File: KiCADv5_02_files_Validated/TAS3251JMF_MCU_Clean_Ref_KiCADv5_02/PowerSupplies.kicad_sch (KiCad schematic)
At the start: 47 parts, among them IC1 LM5010MHX, J18 Conn_01x04, J5 PVDD, J6 Conn_01x01_Male, J7 Conn_01x01_Male, J8 Conn_01x01_Male, J9 Conn_01x01_Male, U2 AMS1117-3.3, U3 LM2940-12

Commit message: adding components
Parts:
- added C54, C55: 1µF, Capacitor_SMD:C_0805_2012Metric_Pad1.15x1.40mm_HandSolder, symbol Device:C
- added D7: D_Schottky_x2_Serial_AKC, Package_TO_SOT_SMD:SOT-23, symbol Device:D_Schottky_x2_Serial_AKC
- added R40: 100k, Resistor_SMD:R_0805_2012Metric_Pad1.15x1.40mm_HandSolder, symbol Device:R
- added R41: 12k, Resistor_SMD:R_0805_2012Metric_Pad1.15x1.40mm_HandSolder, symbol Device:R
- added R42: 3.3k, Resistor_SMD:R_0805_2012Metric_Pad1.15x1.40mm_HandSolder, symbol Device:R
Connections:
- net +12V: now also R41.1
- net +3.3V: now also D7.2 (K)
- net GND: now also C55.2, D7.1 (A), R42.2
- net VDD: now also R40.1
- new net: C54.1, R40.2
- new net POWER UP: C54.2, C55.1, D7.3 (common), R41.2, R42.1
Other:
- note added: "Voltage measurement"
- note added: "for Reset function"

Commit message: Minor changes
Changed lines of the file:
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@@
+		)
+	)
+	(text_box "PVDD 36V\n  ├── LM5010 → 15V\n  │     ├── LM2940-12 → 12V → GVDD_A, GVDD_B\n  │     └── (headroom for future if needed)\n  │\n  ├── LMR33630 (buck #1) → 5V\n  │     ├── TPS7A20-3.3 → 3.3V analog → TAS DAC_AVDD only\n  │     ├── USB-C VBUS power OR node\n  │     ├── spare 5V header/connector\n  │     └── fan connector (optional)\n  │\n  └── LMR33630 (buck #2) → 3.3V digital\n        ├── ESP32-S3\n        ├── STM32F030\n        ├── ADAU1466\n        ├── TAS DAC_DVDD\n        └── AT24C256"
+		(exclude_from_sim no)
+		(at 233.68 163.83 0)
+		(size 68.58 41.91)
+		(margins 0.9525 0.9525 0.9525 0.9525)
+		(stroke
+			(width 0)
+			(type solid)
+		)
+		(fill
+			(type none)
+		)
+		(effects
+			(font
+				(face "Courier New")
+				(size 1.27 1.27)
+			)
+			(justify left top)
 		)
 	)

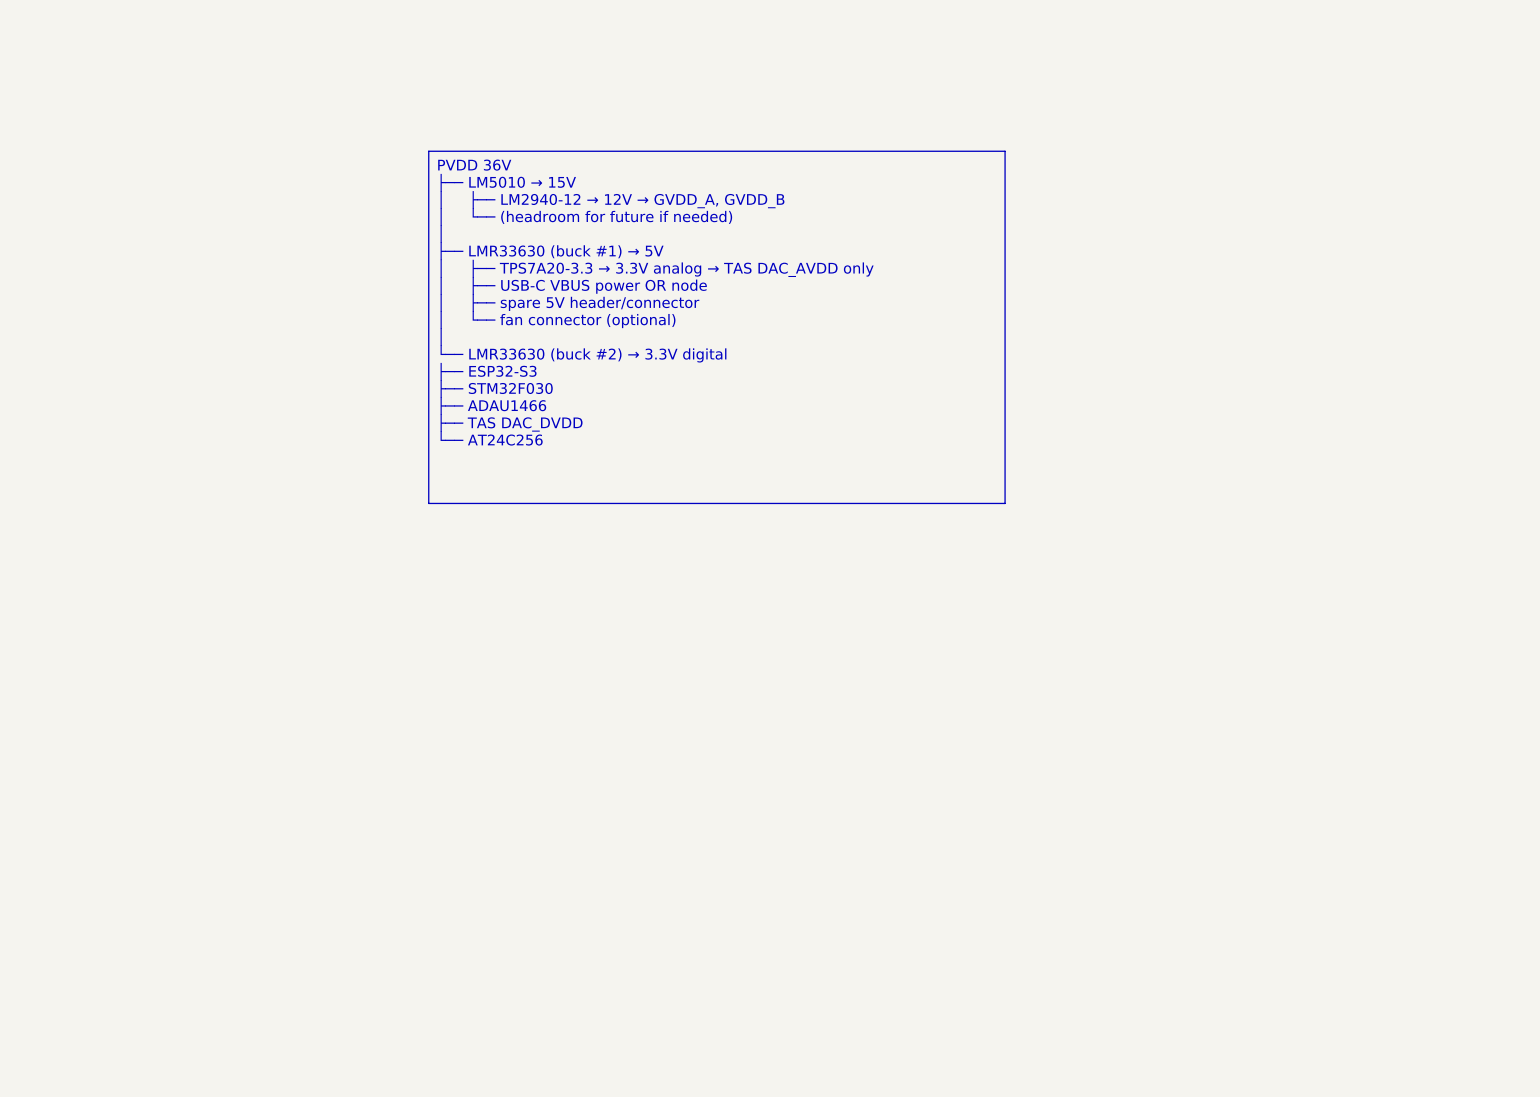
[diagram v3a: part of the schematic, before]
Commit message: Adding signals to control for new uC
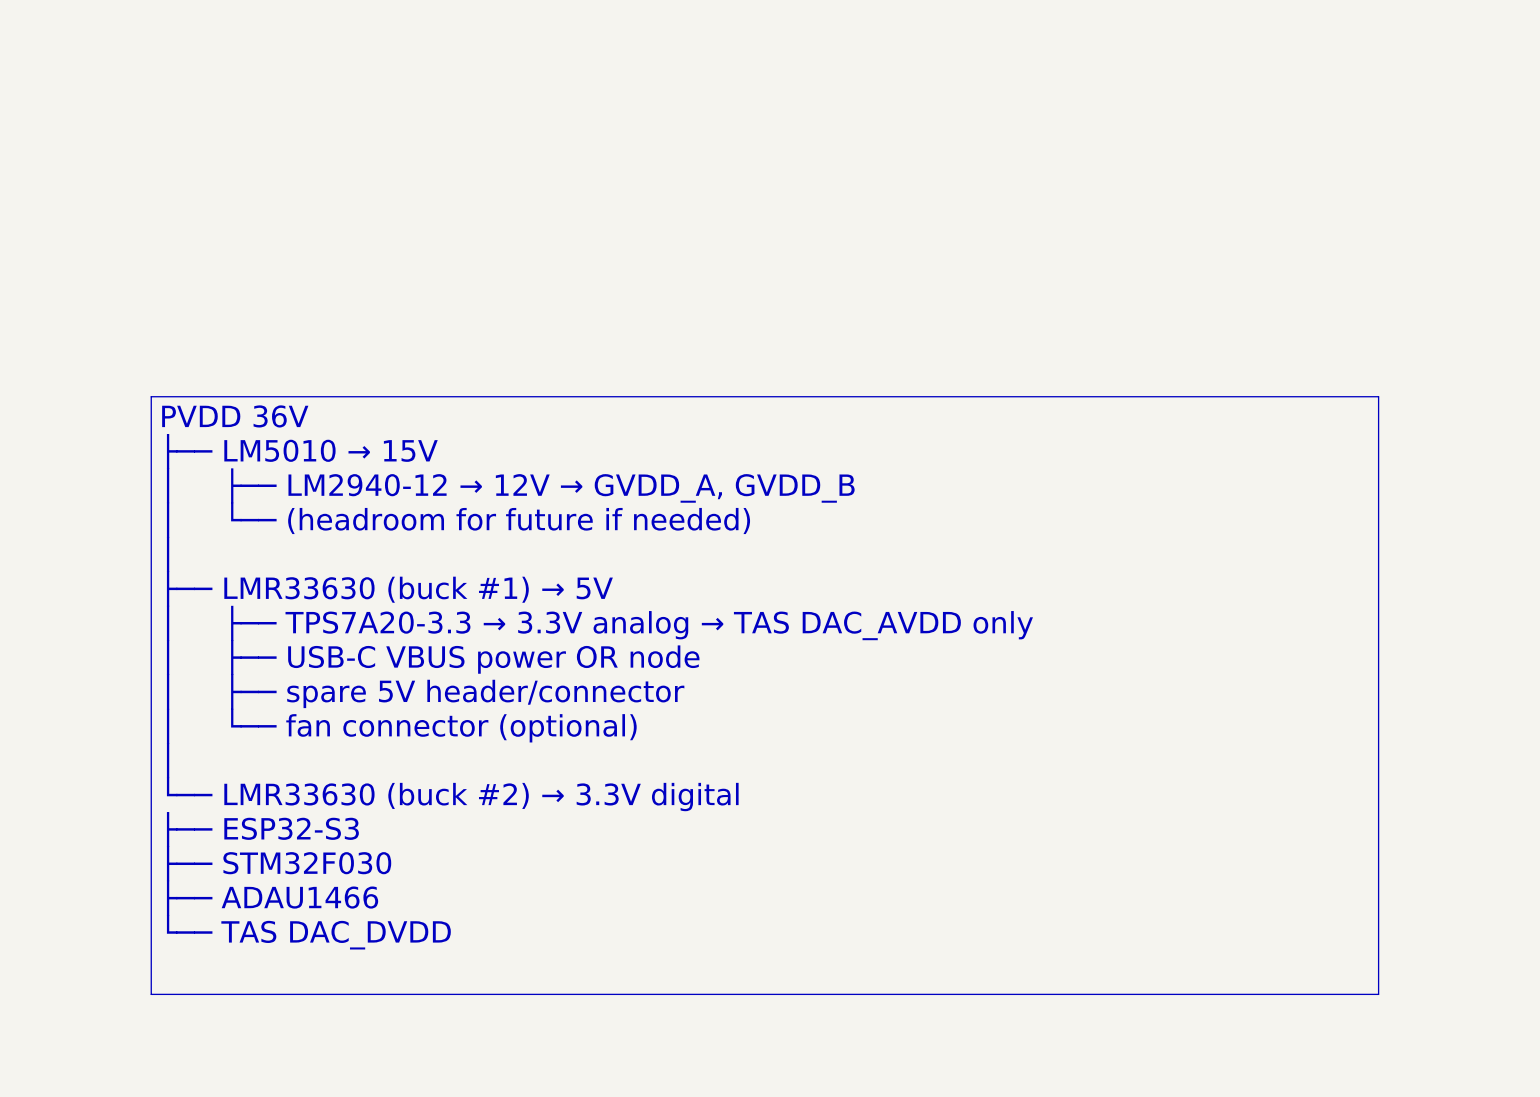
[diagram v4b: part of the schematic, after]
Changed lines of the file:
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@@
 		)
 	)
-	(text_box "PVDD 36V\n  ├── LM5010 → 15V\n  │     ├── LM2940-12 → 12V → GVDD_A, GVDD_B\n  │     └── (headroom for future if needed)\n  │\n  ├── LMR33630 (buck #1) → 5V\n  │     ├── TPS7A20-3.3 → 3.3V analog → TAS DAC_AVDD only\n  │     ├── USB-C VBUS power OR node\n  │     ├── spare 5V header/connector\n  │     └── fan connector (optional)\n  │\n  └── LMR33630 (buck #2) → 3.3V digital\n        ├── ESP32-S3\n        ├── STM32F030\n        ├── ADAU1466\n        ├── TAS DAC_DVDD\n        └── AT24C256"
+	(text_box "PVDD 36V\n  ├── LM5010 → 15V\n  │     ├── LM2940-12 → 12V → GVDD_A, GVDD_B\n  │     └── (headroom for future if needed)\n  │\n  ├── LMR33630 (buck #1) → 5V\n  │     ├── TPS7A20-3.3 → 3.3V analog → TAS DAC_AVDD only\n  │     ├── USB-C VBUS power OR node\n  │     ├── spare 5V header/connector\n  │     └── fan connector (optional)\n  │\n  └── LMR33630 (buck #2) → 3.3V digital\n        ├── ESP32-S3\n        ├── STM32F030\n        ├── ADAU1466\n        └── TAS DAC_DVDD\n"
 		(exclude_from_sim no)
-		(at 233.68 163.83 0)
-		(size 68.58 41.91)
+		(at 200.66 193.04 0)
+		(size 146.05 71.12)
 		(margins 0.9525 0.9525 0.9525 0.9525)
 		(stroke
@@
 			(font
 				(face "Courier New")
-				(size 1.27 1.27)
+				(size 2.54 2.54)
 			)
 			(justify left top)
